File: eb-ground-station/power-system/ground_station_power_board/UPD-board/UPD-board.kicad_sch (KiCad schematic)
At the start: 109 parts, among them J1 Conn_01x04, J10 PI 1827486, J11 Conn_02x02_Odd_Even, J12 Conn_01x05, J2 PC 1720806, J3 Conn_01x03, J4 Conn_01x03, J5 Conn_01x03, J6 Conn_01x03, J7 PI 1924143, J8 PI 1827923, J9 PI 1827486, Q21 SUD50P08-25L-E3, Q22 SUD50P08-25L-E3, U1 MAX7310ATE, U13 dot_small, U18 dot_small, U19 dot_small, U2 MAX7310ATE, U20 dot_small, U21 dot_small, U22 dot_small, U3 MAX7310ATE, U4 MCP9808, U5 ADS1115IDGS, U6 UA78M33, U7 U_RasPi_40pin, U8 dot_small

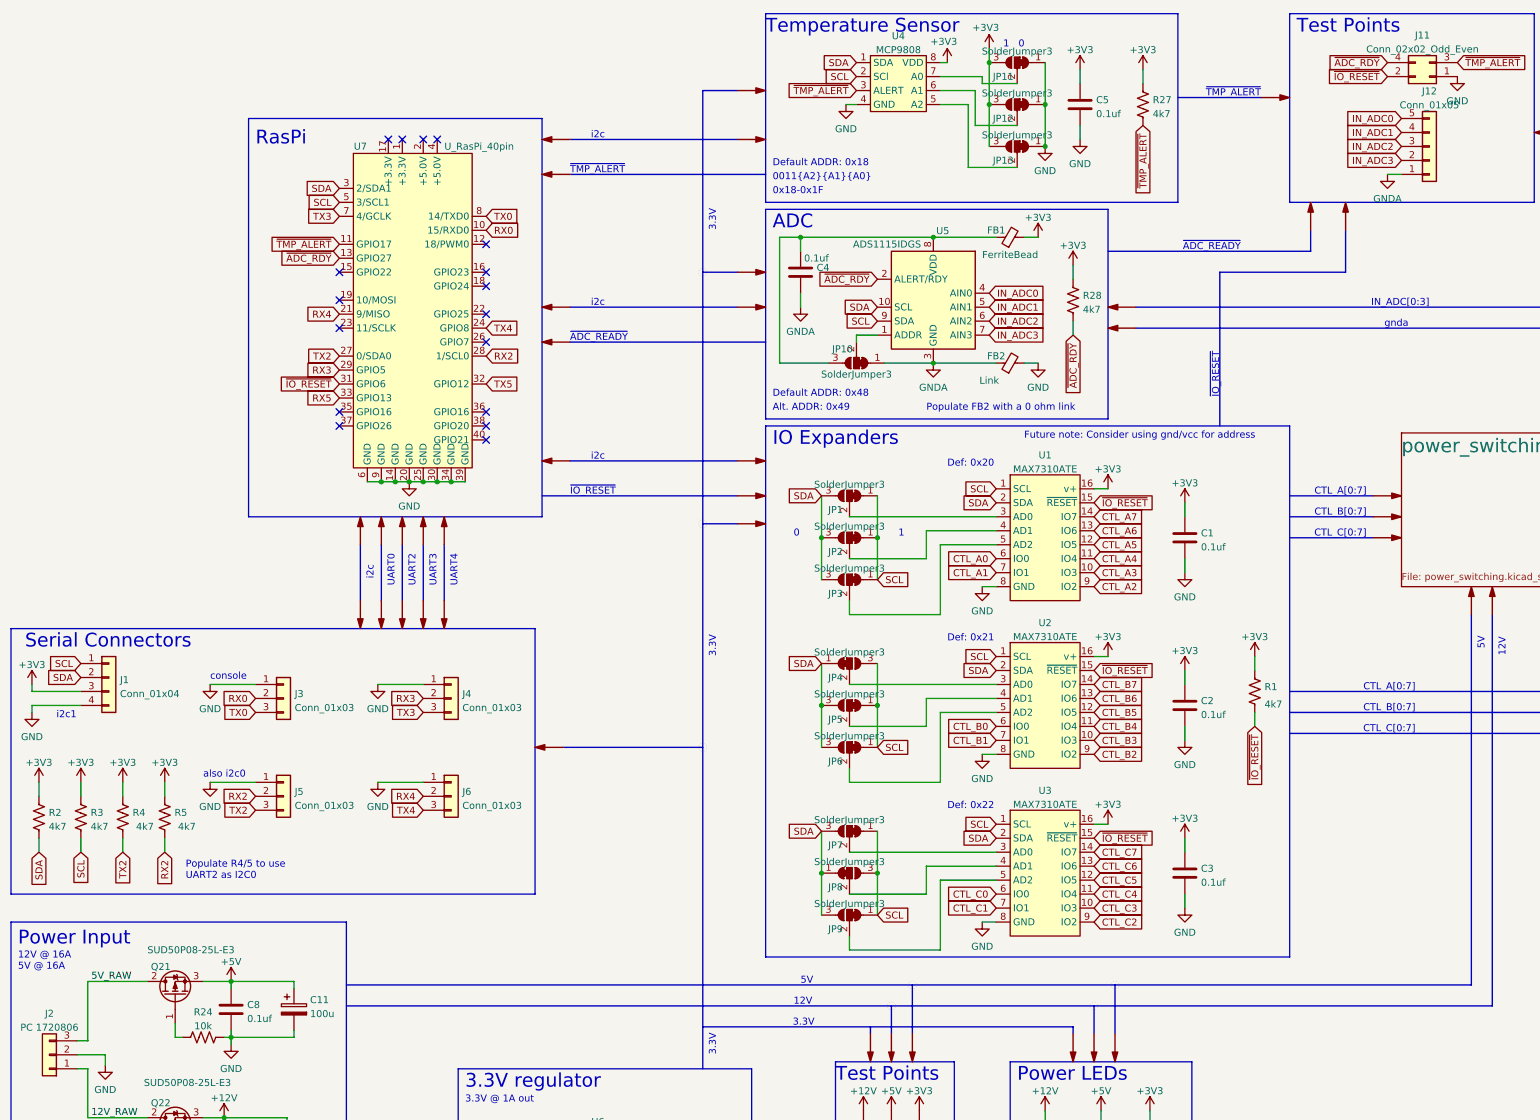
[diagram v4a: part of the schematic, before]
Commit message: Added UART5 breakout pins
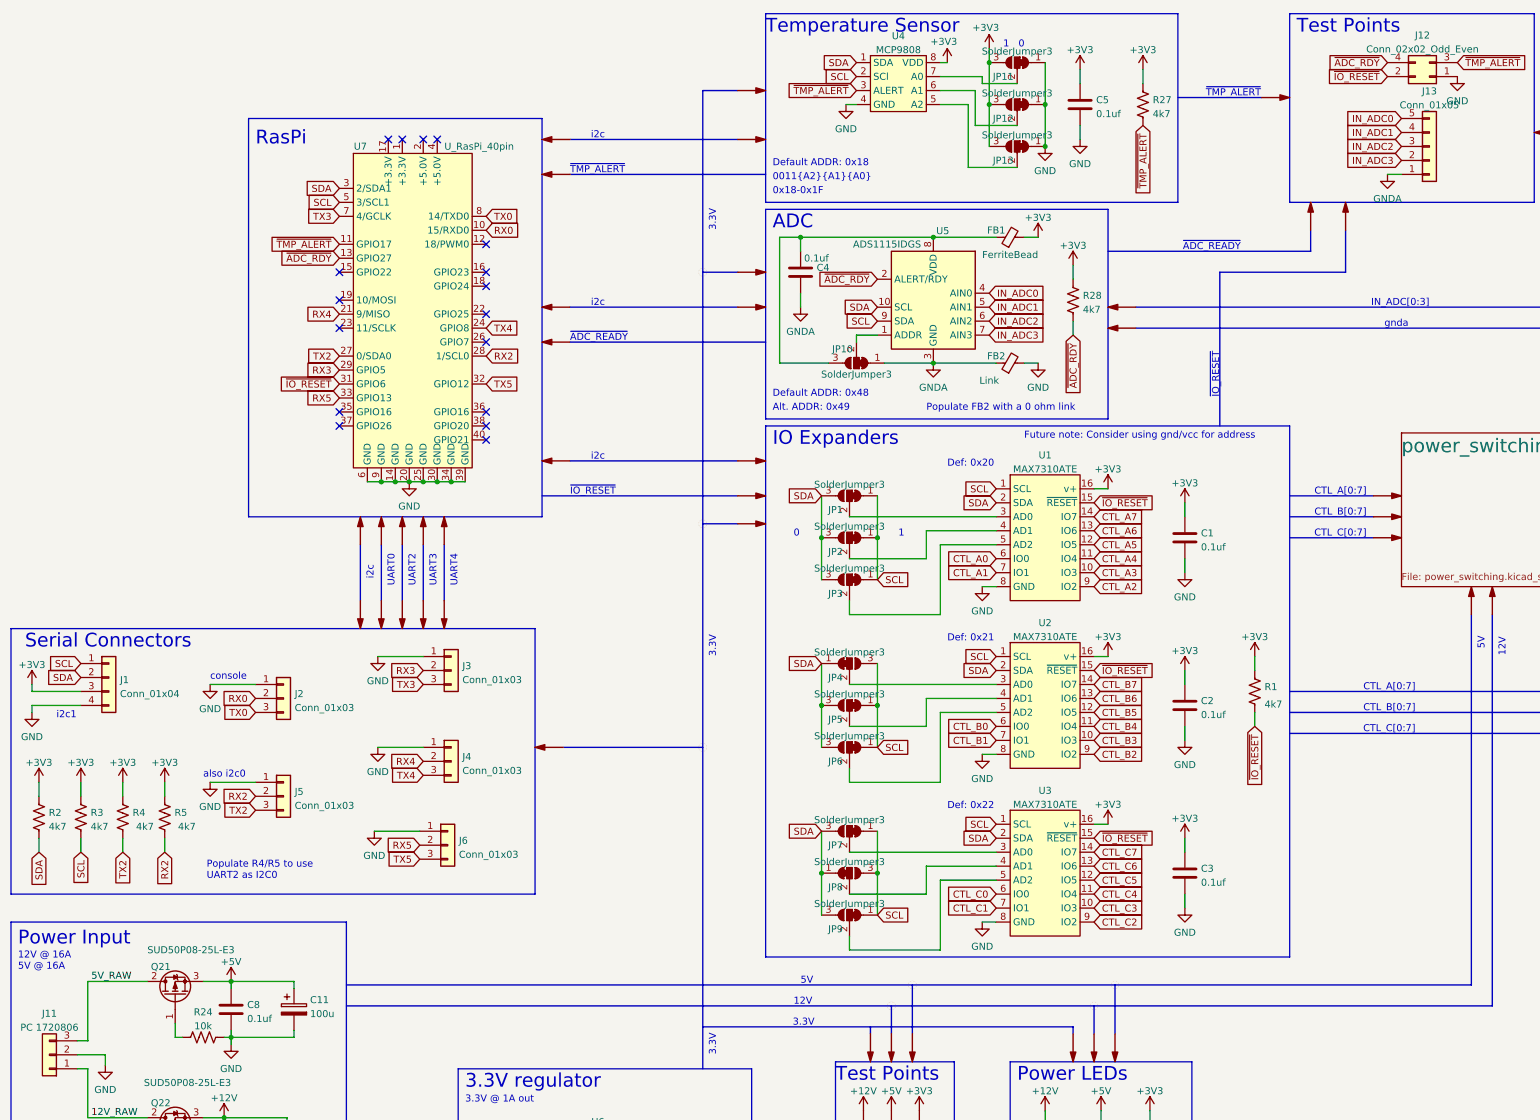
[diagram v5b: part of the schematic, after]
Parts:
- added J6: Conn_01x03, Connector_PinHeader_2.54mm:PinHeader_1x03_P2.54mm_Vertical, symbol Connector_Generic:Conn_01x03
- renumbered J2 to J11, J11 to J12, J12 to J13, J3 to J2, J4 to J3, J6 to J4
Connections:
- net GND: now also J6.1 (Pin_1)
- net RX5: now also J6.2 (Pin_2)
- net TX5: now also J6.3 (Pin_3)
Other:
- note added: "Populate R4/R5 to use UART2 as I2C0"
- note removed: "Populate R4/5 to use UART2 as I2C0"
- company: (none) -> Benjamin Crall
- moved on the sheet: J3, J4

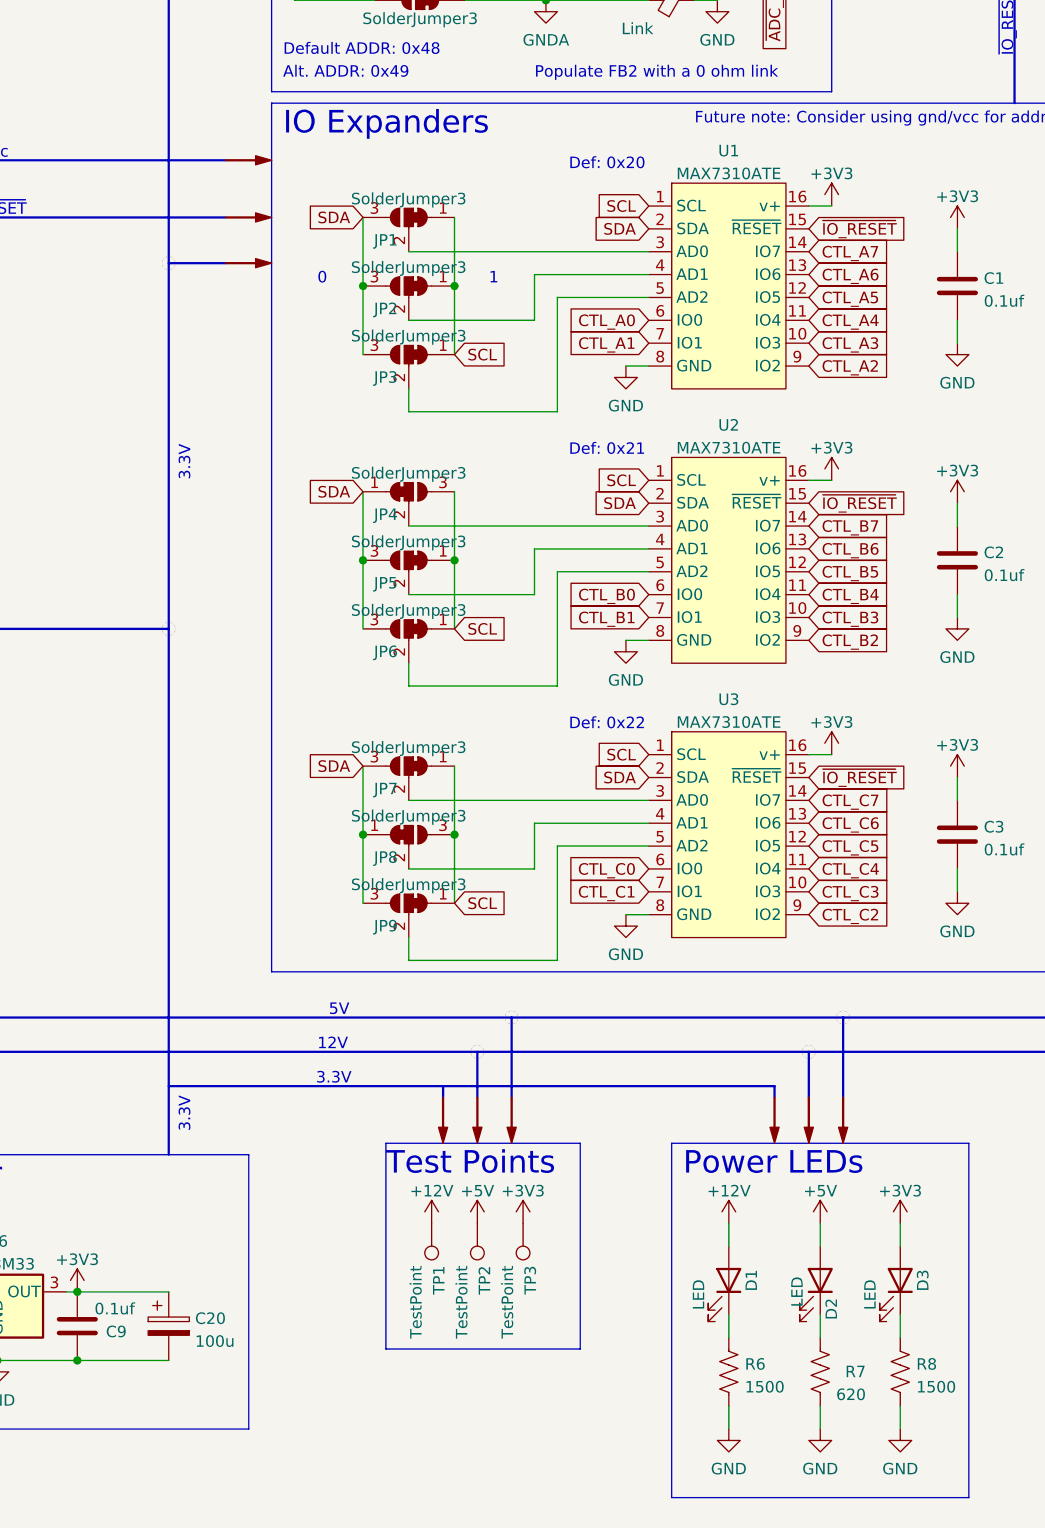
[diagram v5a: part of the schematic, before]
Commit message: Preparing to make changes for unavailable parts
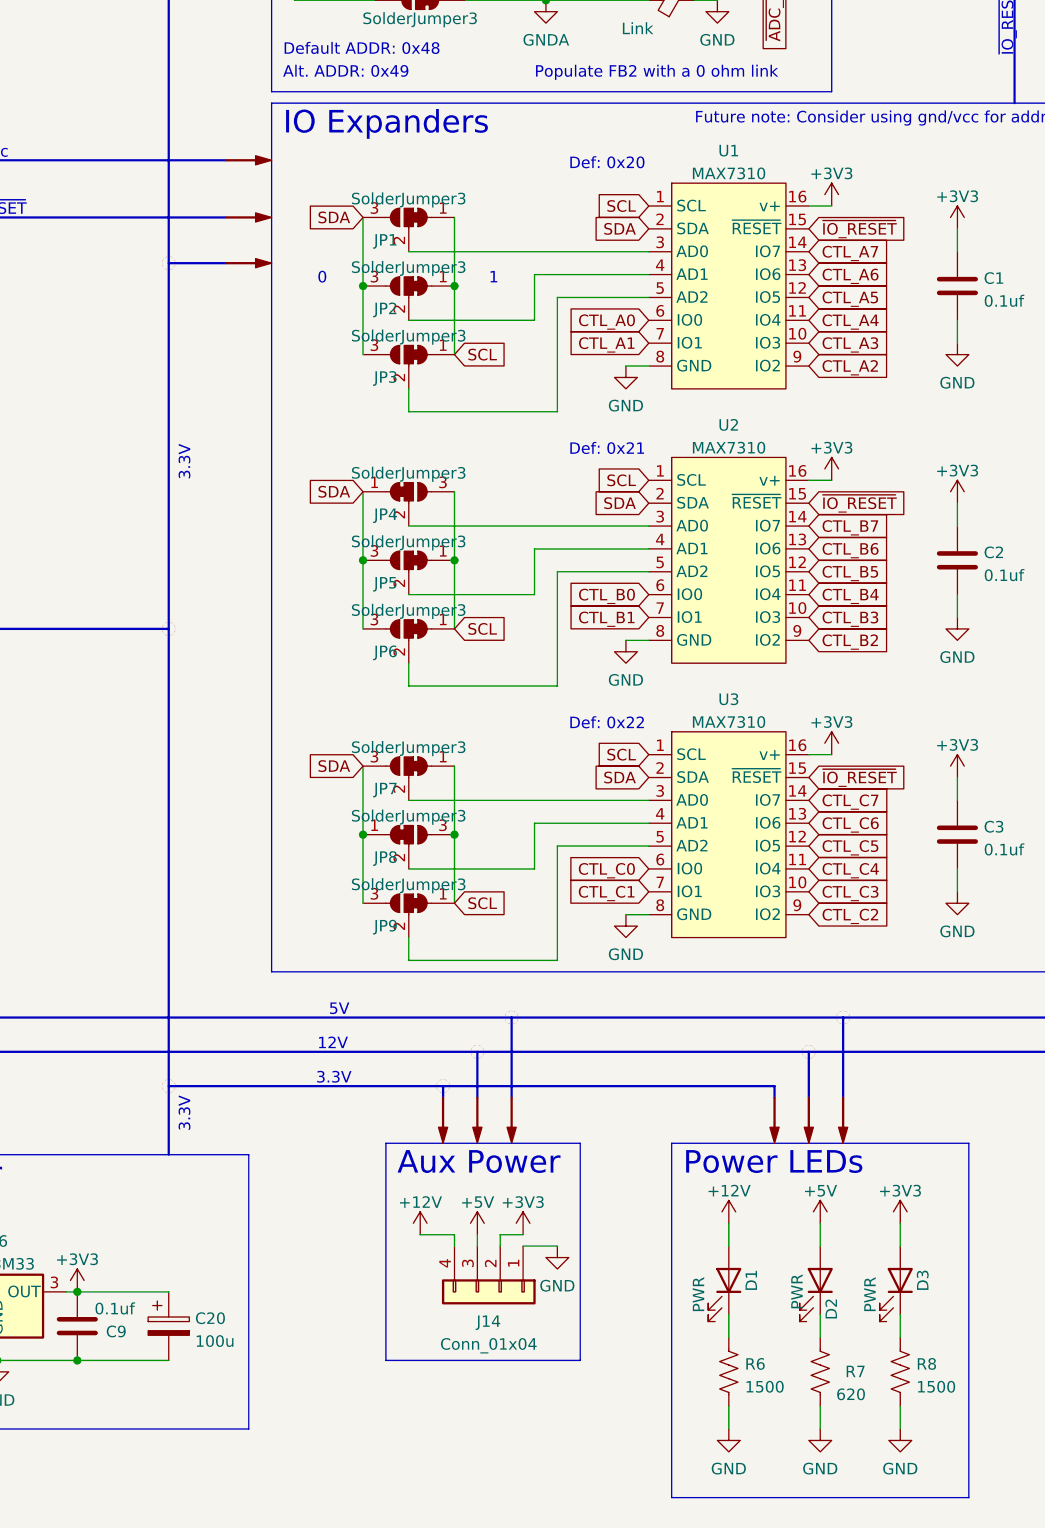
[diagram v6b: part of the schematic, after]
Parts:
- removed TP1, TP2, TP3: TestPoint, oresat-footprints:TestPoint_Pad_1.5x1.5mm, symbol Connector:TestPoint
- removed U13, U18, U19, U20, U21, U22, U8: dot_small, symbol graphics:dot_small
- added J14: Conn_01x04, Connector_PinHeader_2.54mm:PinHeader_1x04_P2.54mm_Vertical, symbol Connector_Generic:Conn_01x04
- C1, C10, C11, C2, C20, C3, C4, C5, C6, C7, C8, C9: Distributor (none) -> DigiKey
- D1, D2, D3: value LED -> PWR
- FB1, FB3: footprint oresat-footprints:1206-or-0805 -> Capacitor_SMD:C_0805_2012Metric; Distributor (none) -> DigiKey
- FB2: footprint oresat-footprints:1206-or-0805 -> Resistor_SMD:R_0805_2012Metric
- U1, U2, U3: value MAX7310ATE -> MAX7310; DPN (none) -> 700-MAX7310ATET; Distributor (none) -> Mouser; MPN (none) -> MAX7310ATE+T; Mfr (none) -> Maxim Integrated
- U4, U5: Distributor (none) -> no one :(
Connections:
- net +12V: now also J14.4 (Pin_4)
- net +3V3: now also J14.2 (Pin_2)
- net +5V: now also J14.3 (Pin_3)
- net GND: now also J14.1 (Pin_1)
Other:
- note added: "Aux Power"
- title: Uniclogs Power Distribution Board -> UniClOGS Power Distribution Board

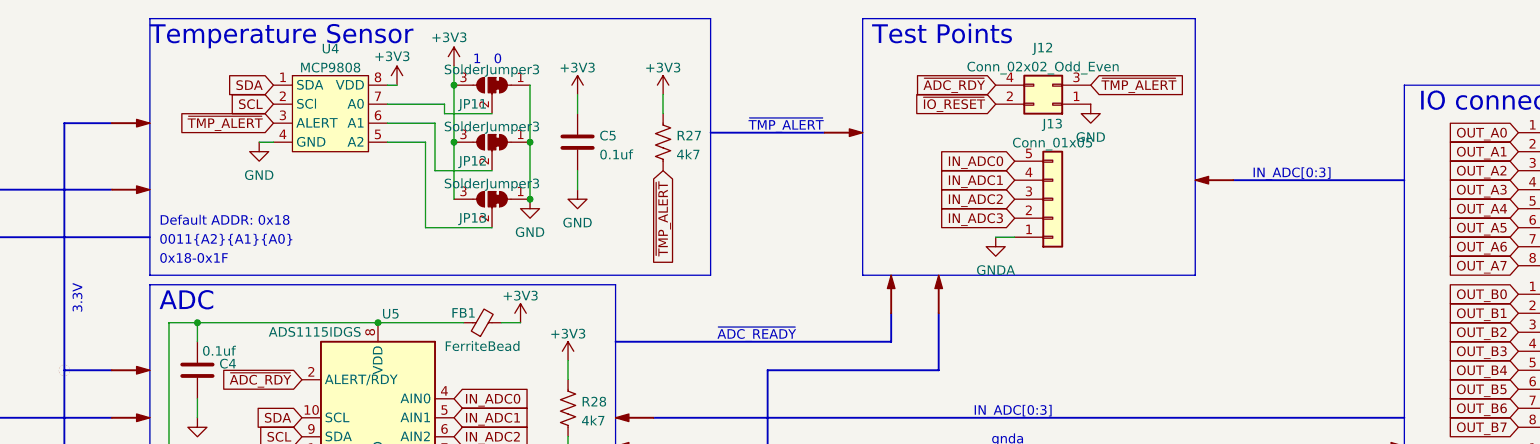
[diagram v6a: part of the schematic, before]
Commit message: Fixed silkscreen and switched components
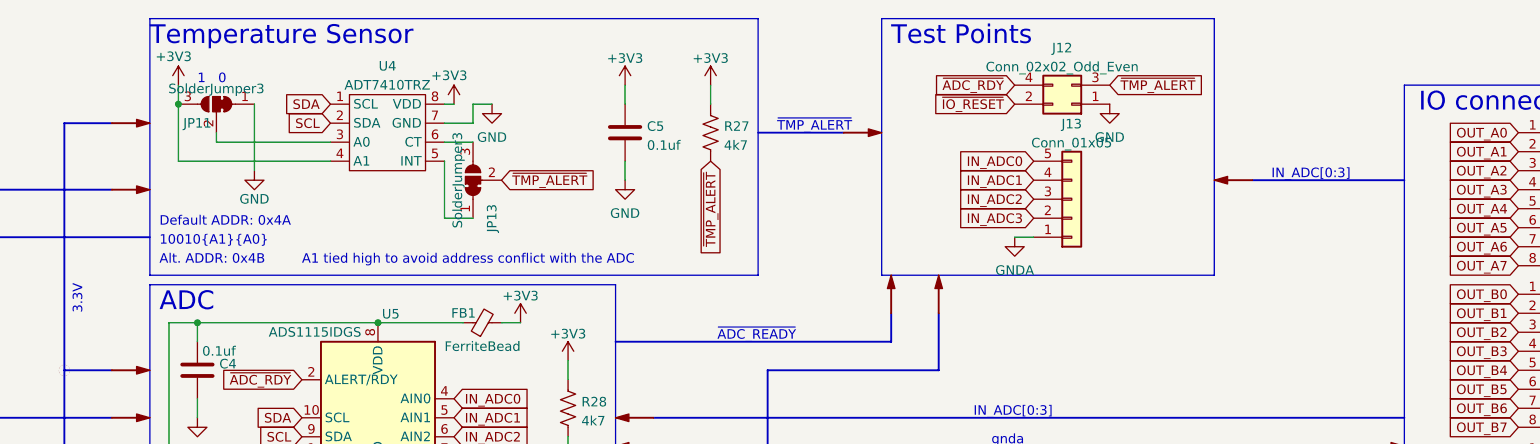
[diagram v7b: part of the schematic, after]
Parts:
- removed JP12: SolderJumper3, oresat-footprints:SolderJumper-3_P1.3mm_Bridged12_Pad1.0x1.5mm, symbol Jumper:SolderJumper_3_Bridged12
- removed U4: MCP9808, Package_SO:MSOP-8_3x3mm_P0.65mm, symbol OreSat-U-MCP9808-i2c-temperature:MCP9808
- added U4: ADT7410TRZ, Package_SO:SOIC-8_3.9x4.9mm_P1.27mm, symbol OreSat-U-ADT7410TRZ-i2c-temperature:ADT7410TRZ
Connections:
- net +3V3: now also U4.4 (A1), U4.8 (VDD); no longer JP13.3 (B)
- net GND: now also U4.7 (GND); no longer JP13.1 (A)
- net SCL: now also U4.2 (SDA)
- net SDA: now also U4.1 (SCL)
- net ~{TMP_ALERT}: now also JP13.2 (C)
- net at JP11.2 (C): now also U4.3 (A0)
- new net: JP13.1 (A), U4.5 (INT)
- new net: JP13.3 (B), U4.6 (CT)
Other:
- note added: "10010{A1}{A0}"
- note added: "A1 tied high to avoid address conflict with the ADC"
- note added: "Alt. ADDR: 0x4B"
- note added: "Default ADDR: 0x4A"
- note removed: "0011{A2}{A1}{A0}"
- note removed: "0x18-0x1F"
- note removed: "Default ADDR: 0x18"
- moved on the sheet: C5, J12, J13, JP11, JP13, R27
